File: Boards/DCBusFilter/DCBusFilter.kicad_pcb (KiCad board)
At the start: 4 copper layers, 89 x 85 mm, 15 parts, among them J1 TBP01R2-508-04BE

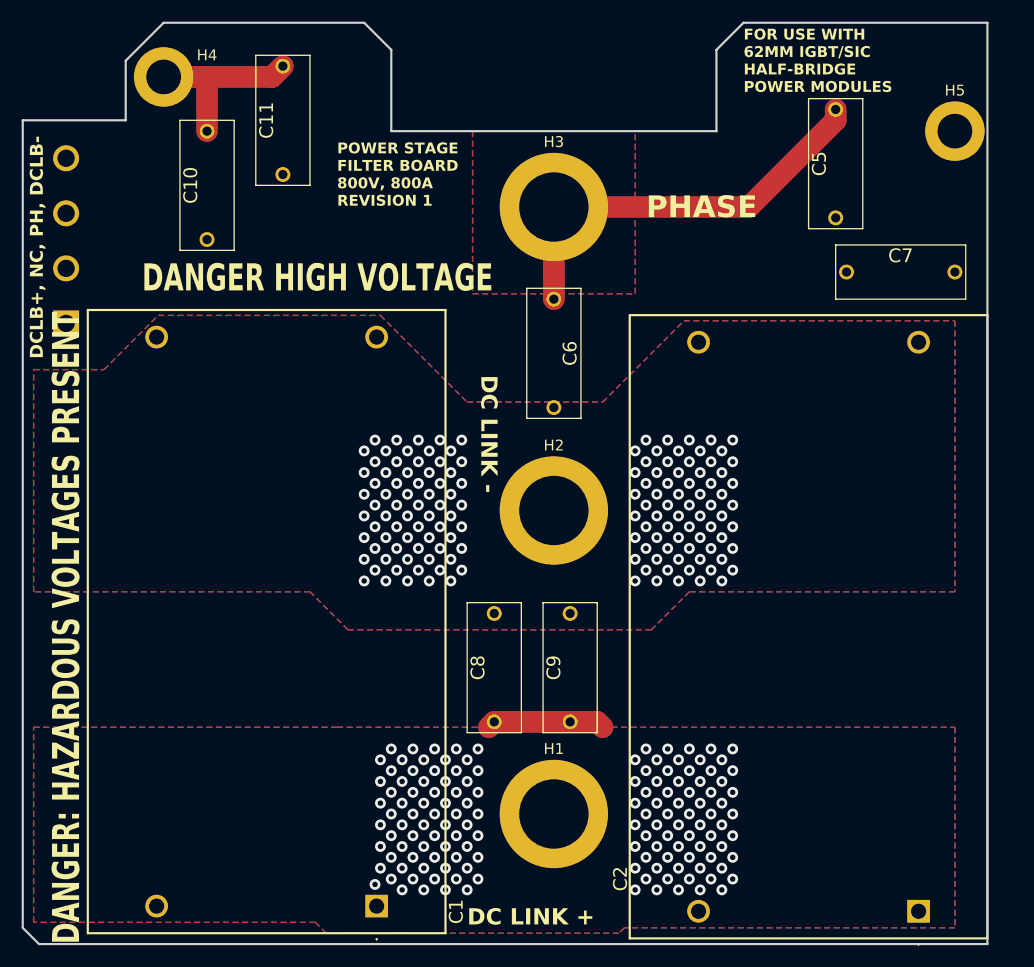
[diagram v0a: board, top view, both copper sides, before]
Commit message: Update Silscreen for variants, fix gate driver and remove todo
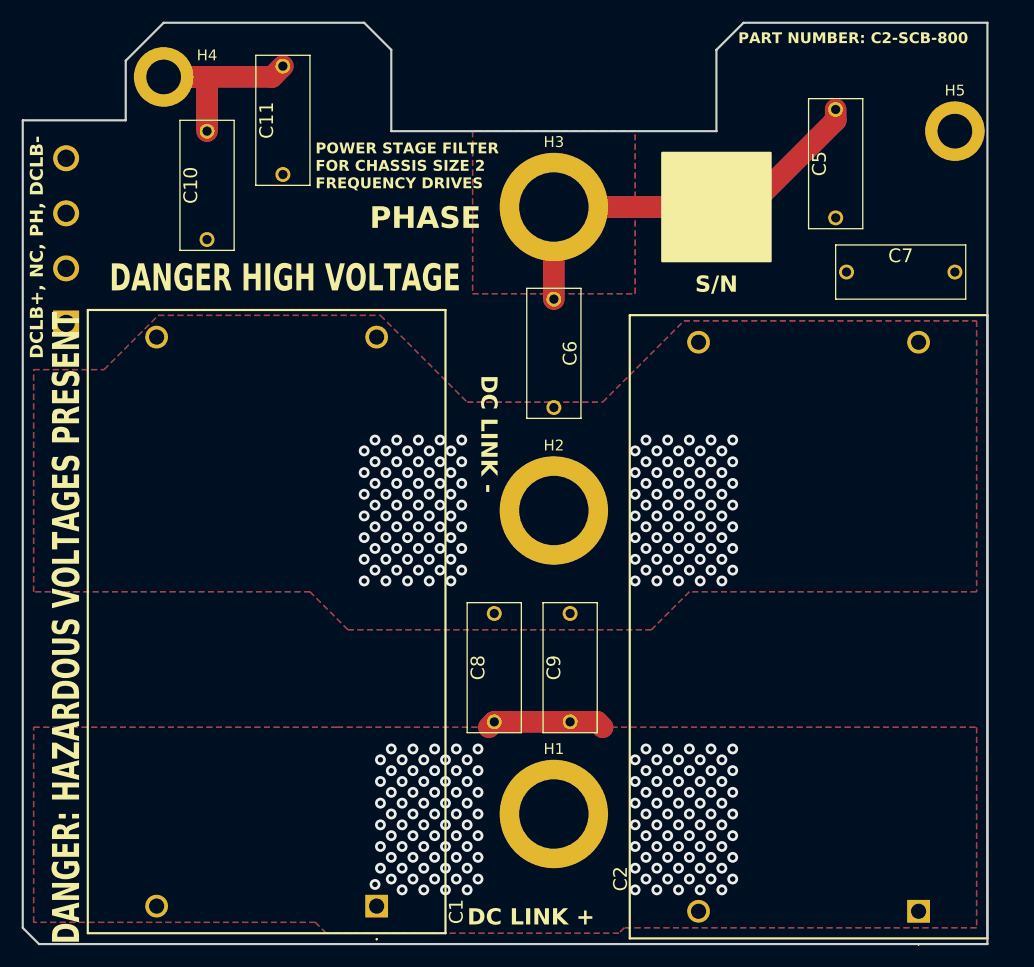
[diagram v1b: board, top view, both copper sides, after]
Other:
- board text added: "PART NUMBER: C2-SCB-800"
- board text added: "POWER STAGE FILTER FOR CHASSIS SIZE 2 FREQUENCY DRIVES"
- board text added: "S/N"
- board text removed: "POWER STAGE FILTER BOARD 800V, 800A REVISION 1"
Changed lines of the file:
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@@
 			(outputformat 1)
 			(mirror no)
-			(drillshape 1)
+			(drillshape 0)
 			(scaleselection 1)
-			(outputdirectory "")
+			(outputdirectory "Fab/")
 		)
 	)
@@
 	)
 	(gr_rect
-		(start 0 27.5)
-		(end 90 42.5)
+		(start 2 27.5)
+		(end 89 42.5)
 		(stroke
 			(width 0.2)
@@
 		)
 		(fill yes)
-		(locked yes)
 		(layer "B.Mask")
 	)
@@
 	)
 	(gr_rect
-		(start 0 57)
-		(end 90 70)
+		(start 2 57)
+		(end 89 70)
 		(stroke
 			(width 0.2)
@@
 		(layer "B.Mask")
 	)
+	(gr_rect
+		(start 60 2)
+		(end 70 12)
+		(stroke
+			(width 0.2)
+			(type solid)
+		)
+		(fill yes)
+		(layer "F.SilkS")
+	)
 	(gr_poly
 		(pts
@@
 		(layer "Edge.Cuts")
 	)
-	(gr_text "FOR USE WITH\n62MM IGBT/SIC\nHALF-BRIDGE\nPOWER MODULES"
-		(at 67.5 -3.5 0)
+	(gr_text "PART NUMBER: C2-SCB-800"
+		(at 67 -8 0)
 		(layer "F.SilkS")
 		(effects
@@
 		)
 	)
+	(gr_text "S/N"
+		(at 65 15 0)
+		(layer "F.SilkS")
+		(effects
+			(font
+				(size 1.5 1.5)
+				(thickness 0.3)
+				(bold yes)
+			)
+			(justify bottom)
+		)
+	)
 	(gr_text "DANGER: HAZARDOUS VOLTAGES PRESENT"
 		(at 6.5 75 90)
@@
 	)
 	(gr_text "PHASE"
-		(at 58.5 7 0)
+		(at 33 8 0)
 		(layer "F.SilkS")
 		(effects
@@
 	)
 	(gr_text "DANGER HIGH VOLTAGE"
-		(at 12 15 0)
+		(at 9 15 0)
 		(layer "F.SilkS" knockout)
 		(effects
@@
 		)
 	)
-	(gr_text "POWER STAGE\nFILTER BOARD\n800V, 800A\nREVISION 1"
-		(at 30 1 0)
+	(gr_text "POWER STAGE FILTER\nFOR CHASSIS SIZE 2\nFREQUENCY DRIVES"
+		(at 28 1 0)
 		(layer "F.SilkS")
 		(effects
@@
 		(polygon
 			(pts
-				(xy 2 55) (xy 30 55) (xy 30 55) (xy 50 55) (xy 60 55) (xy 60 55) (xy 87 55) (xy 87 73.5) (xy 56.5 73.5)
-				(xy 56 74) (xy 29 74) (xy 28 73) (xy 2 73)
+				(xy 2 55) (xy 30 55) (xy 50 55) (xy 60 55) (xy 89 55) (xy 89 73.5) (xy 56.5 73.5) (xy 56 74) (xy 29 74)
+				(xy 28 73) (xy 2 73)
 			)
 		)
@@
 		(polygon
 			(pts
-				(xy 2 22) (xy 8.5 22) (xy 13.5 17) (xy 34 17) (xy 42 25) (xy 54.5 25) (xy 62 17.5) (xy 87 17.5)
-				(xy 87 42.5) (xy 62.5 42.5) (xy 59 46) (xy 31 46) (xy 27.5 42.5) (xy 2 42.5)
+				(xy 2 22) (xy 8.5 22) (xy 13.5 17) (xy 34 17) (xy 42 25) (xy 54.5 25) (xy 62 17.5) (xy 89 17.5)
+				(xy 89 42.5) (xy 62.5 42.5) (xy 59 46) (xy 31 46) (xy 27.5 42.5) (xy 2 42.5)
 			)
 		)
